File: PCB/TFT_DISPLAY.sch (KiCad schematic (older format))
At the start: 7 parts, among them Q5 MMBT4401-7-F, U17 DT024CTFT(-TS), U18 74HC245, U19 74HC245

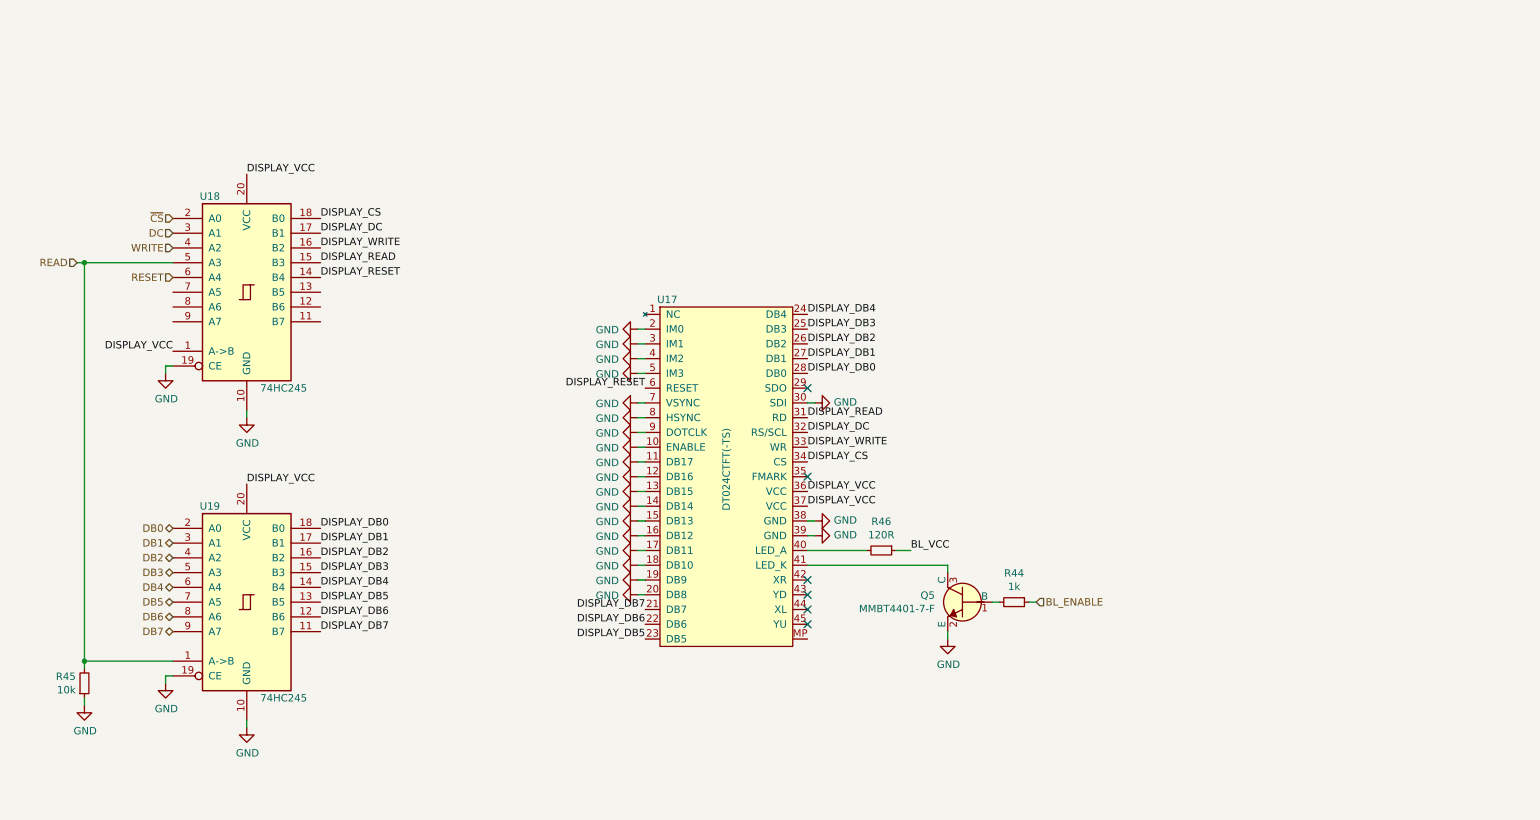
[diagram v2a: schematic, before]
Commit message: Added decoupling and voltage regulation
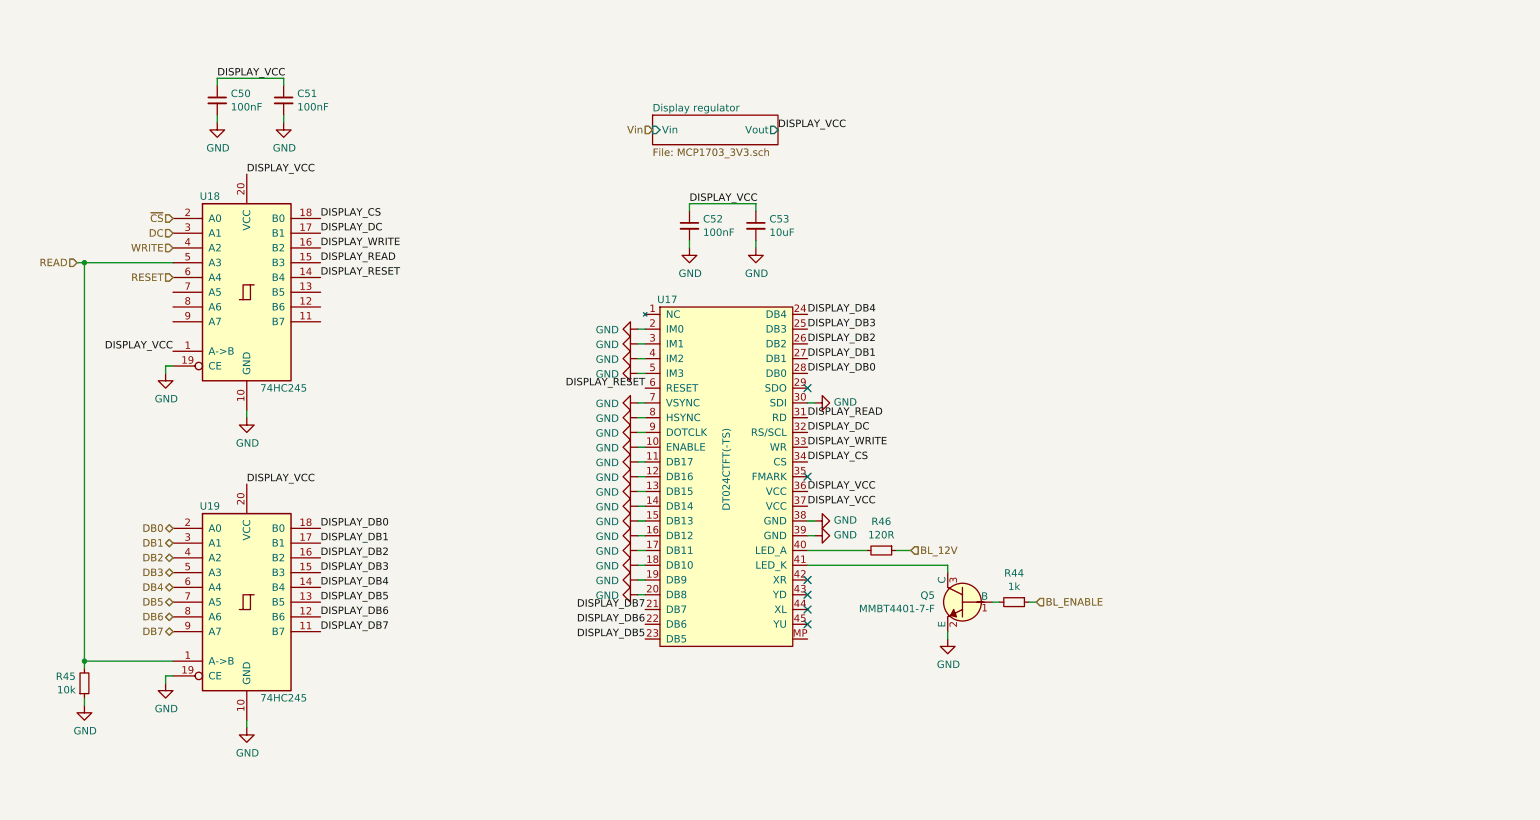
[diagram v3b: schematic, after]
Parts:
- added C50, C51, C52: 100nF, symbol Device:C_Small
- added C53: 10uF, symbol Device:C_Small
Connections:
- net DISPLAY_VCC: now also C50.1, C51.1, C52.1, C53.1
- net GND: now also C50.2, C51.2, C52.2, C53.2
- net BL_VCC renamed BL_12V
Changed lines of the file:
@@
 $Descr A4 11693 8268
 encoding utf-8
-Sheet 27 27
+Sheet 27 28
 Title ""
 Date ""
@@
 NoConn ~ 6850 4750
 NoConn ~ 6850 4850
-Text Label 7550 4350 0    50   ~ 0
-BL_VCC
 $Comp
 L power:GND #PWR0165
@@
 Wire Wire Line
 	6850 4350 7250 4350
+Text Label 6650 1500 0    50   ~ 0
+DISPLAY_VCC
+$Sheet
+S 5800 1400 850  200
+U 5EA9342A
+F0 "Display regulator" 50
+F1 "MCP1703_3V3.sch" 50
+F2 "Vin" I L 5800 1500 50
+F3 "Vout" O R 6650 1500 50
+$EndSheet
+Text HLabel 7550 4350 2    50   Input ~ 0
+BL_12V
+Wire Wire Line
+	2850 1150 3300 1150
+Wire Wire Line
+	2850 1400 2850 1450
+$Comp
+L power:GND #PWR0183
+U 1 1 5EAA8FA4
+P 2850 1450
+F 0 "#PWR0183" H 2850 1200 50  0001 C CNN
+F 1 "GND" H 2855 1277 50  0000 C CNN
+F 2 "" H 2850 1450 50  0001 C CNN
+F 3 "" H 2850 1450 50  0001 C CNN
+	1    2850 1450
+	1    0    0    -1
+$EndComp
+Wire Wire Line
+	2850 1150 2850 1200
+$Comp
+L Device:C_Small C50
+U 1 1 5EAA8F9C
+P 2850 1300
+F 0 "C50" H 2942 1346 50  0000 L CNN
+F 1 "100nF" H 2942 1255 50  0000 L CNN
+F 2 "" H 2850 1300 50  0001 C CNN
+F 3 "~" H 2850 1300 50  0001 C CNN
+	1    2850 1300
+	1    0    0    -1
+$EndComp
+Wire Wire Line
+	3300 1400 3300 1450
+$Comp
+L power:GND #PWR0184
+U 1 1 5EAA64C6
+P 3300 1450
+F 0 "#PWR0184" H 3300 1200 50  0001 C CNN
+F 1 "GND" H 3305 1277 50  0000 C CNN
+F 2 "" H 3300 1450 50  0001 C CNN
+F 3 "" H 3300 1450 50  0001 C CNN
+	1    3300 1450
+	1    0    0    -1
+$EndComp
+Wire Wire Line
+	3300 1150 3300 1200
+Text Label 2850 1150 0    50   ~ 0
+DISPLAY_VCC
+$Comp
+L Device:C_Small C51
+U 1 1 5EAA43F9
+P 3300 1300
+F 0 "C51" H 3392 1346 50  0000 L CNN
+F 1 "100nF" H 3392 1255 50  0000 L CNN
+F 2 "" H 3300 1300 50  0001 C CNN
+F 3 "~" H 3300 1300 50  0001 C CNN
+	1    3300 1300
+	1    0    0    -1
+$EndComp
+Wire Wire Line
+	6050 2000 6500 2000
+Wire Wire Line
+	6050 2250 6050 2300
+$Comp
+L power:GND #PWR0185
+U 1 1 5EAB867A
+P 6050 2300
+F 0 "#PWR0185" H 6050 2050 50  0001 C CNN
+F 1 "GND" H 6055 2127 50  0000 C CNN
+F 2 "" H 6050 2300 50  0001 C CNN
+F 3 "" H 6050 2300 50  0001 C CNN
+	1    6050 2300
+	1    0    0    -1
+$EndComp
+Wire Wire Line
+	6050 2000 6050 2050
+$Comp
+L Device:C_Small C52
+U 1 1 5EAB8681
+P 6050 2150
+F 0 "C52" H 6142 2196 50  0000 L CNN
+F 1 "100nF" H 6142 2105 50  0000 L CNN
+F 2 "" H 6050 2150 50  0001 C CNN
+F 3 "~" H 6050 2150 50  0001 C CNN
+	1    6050 2150
+	1    0    0    -1
+$EndComp
+Wire Wire Line
+	6500 2250 6500 2300
+$Comp
+L power:GND #PWR0186
+U 1 1 5EAB8688
+P 6500 2300
+F 0 "#PWR0186" H 6500 2050 50  0001 C CNN
+F 1 "GND" H 6505 2127 50  0000 C CNN
+F 2 "" H 6500 2300 50  0001 C CNN
+F 3 "" H 6500 2300 50  0001 C CNN
+	1    6500 2300
+	1    0    0    -1
+$EndComp
+Wire Wire Line
+	6500 2000 6500 2050
+Text Label 6050 2000 0    50   ~ 0
+DISPLAY_VCC
+$Comp
+L Device:C_Small C53
+U 1 1 5EAB8690
+P 6500 2150
+F 0 "C53" H 6592 2196 50  0000 L CNN
+F 1 "10uF" H 6592 2105 50  0000 L CNN
+F 2 "" H 6500 2150 50  0001 C CNN
+F 3 "~" H 6500 2150 50  0001 C CNN
+	1    6500 2150
+	1    0    0    -1
+$EndComp
+Text HLabel 5800 1500 0    50   Input ~ 0
+Vin
 $EndSCHEMATC

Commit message: Corrected bus driver MPNs
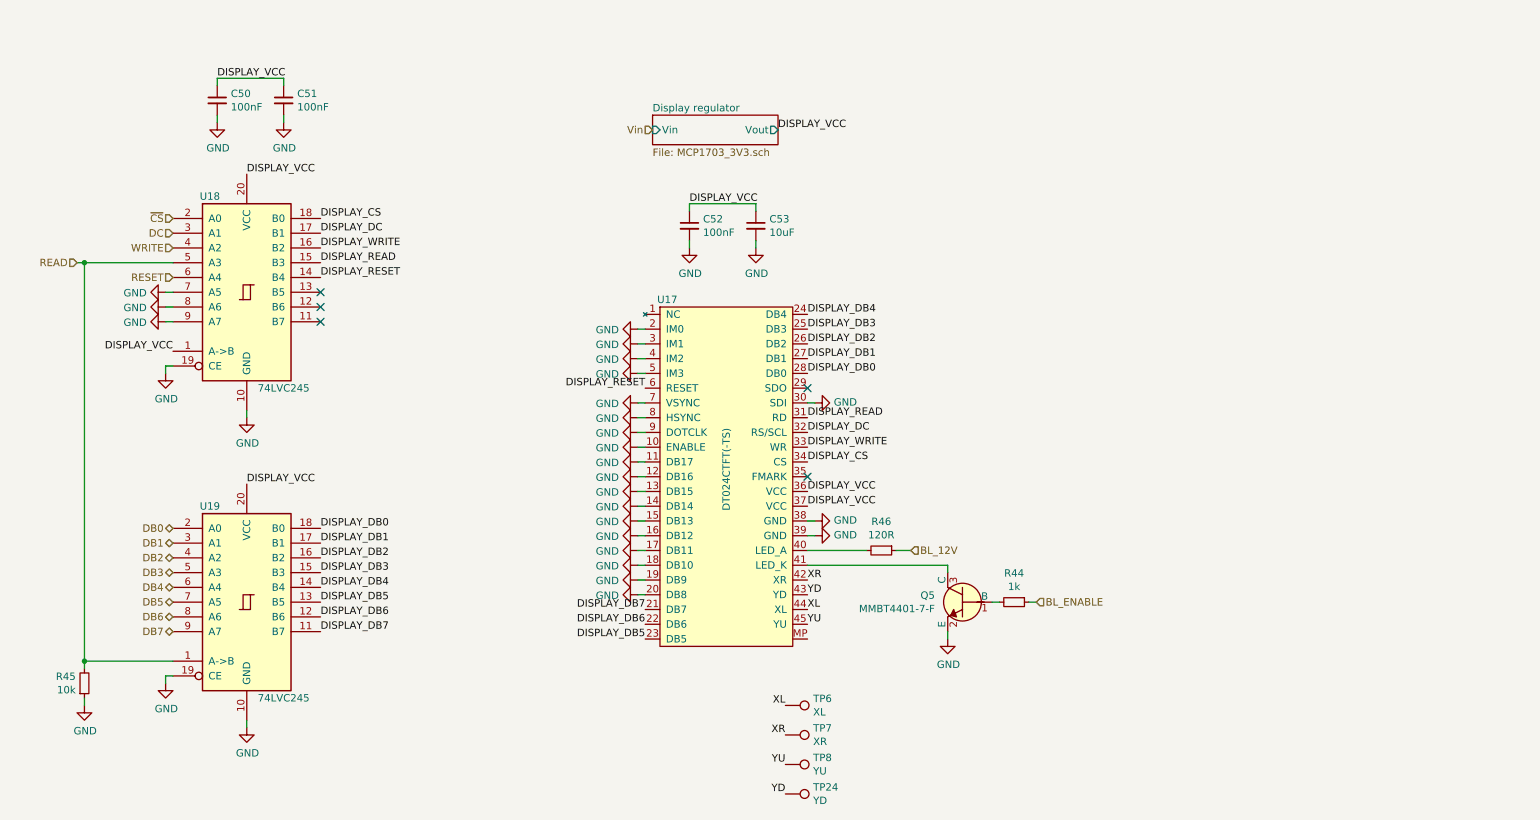
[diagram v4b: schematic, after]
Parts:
- added TP24: YD, symbol Connector:TestPoint
- added TP6: XL, symbol Connector:TestPoint
- added TP7: XR, symbol Connector:TestPoint
- added TP8: YU, symbol Connector:TestPoint
- U18, U19: value 74HC245 -> 74LVC245
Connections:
- net GND: now also U18.7 (A5), U18.8 (A6), U18.9 (A7)
- net XR: now reaches U17.42 (XR)
- net XR: now also TP7.1
- net YD: now reaches U17.43 (YD)
- net YD: now also TP24.1
- net XL: now reaches U17.44 (XL)
- net XL: now also TP6.1
- net YU: now reaches U17.45 (YU)
- net YU: now also TP8.1
- no-connect marks 6 -> 5
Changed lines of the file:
@@
 DISPLAY_VCC
-$Comp
-L 74xx:74HC245 U19
-U 1 1 5E9F8F76
-P 3050 4700
-F 0 "U19" H 2800 5350 50  0000 C CNN
-F 1 "74HC245" H 3300 4050 50  0000 C CNN
-F 2 "" H 3050 4700 50  0001 C CNN
-F 3 "http://www.ti.com/lit/gpn/sn74HC245" H 3050 4700 50  0001 C CNN
-	1    3050 4700
-	1    0    0    -1
-$EndComp
 $Comp
 L power:GND #PWR0158
@@
 P 3050 2600
 F 0 "U18" H 2800 3250 50  0000 C CNN
-F 1 "74HC245" H 3300 1950 50  0000 C CNN
+F 1 "74LVC245" H 3300 1950 50  0000 C CNN
 F 2 "" H 3050 2600 50  0001 C CNN
-F 3 "http://www.ti.com/lit/gpn/sn74HC245" H 3050 2600 50  0001 C CNN
+F 3 "http://www.ti.com/lit/ds/symlink/sn74lvc245a.pdf" H 3050 2600 50  0001 C CNN
 	1    3050 2600
 	1    0    0    -1
@@
 Text Label 2550 3000 2    50   ~ 0
 DISPLAY_VCC
-NoConn ~ 6850 4550
-NoConn ~ 6850 4650
-NoConn ~ 6850 4750
-NoConn ~ 6850 4850
 $Comp
 L power:GND #PWR0165
@@
 Text HLabel 5800 1500 0    50   Input ~ 0
 Vin
+$Comp
+L 74xx:74HC245 U19
+U 1 1 5E9F8F76
+P 3050 4700
+F 0 "U19" H 2800 5350 50  0000 C CNN
+F 1 "74LVC245" H 3300 4050 50  0000 C CNN
+F 2 "" H 3050 4700 50  0001 C CNN
+F 3 "http://www.ti.com/lit/ds/symlink/sn74lvc245a.pdf" H 3050 4700 50  0001 C CNN
+	1    3050 4700
+	1    0    0    -1
+$EndComp
+$Comp
+L Connector:TestPoint TP7
+U 1 1 5EADCDE5
+P 6700 5600
+F 0 "TP7" V 6654 5788 50  0000 L CNN
+F 1 "XR" V 6745 5788 50  0000 L CNN
+F 2 "" H 6900 5600 50  0001 C CNN
+F 3 "~" H 6900 5600 50  0001 C CNN
+	1    6700 5600
+	0    1    1    0
+$EndComp
+$Comp
+L Connector:TestPoint TP6
+U 1 1 5EADD33B
+P 6700 5400
+F 0 "TP6" V 6654 5588 50  0000 L CNN
+F 1 "XL" V 6745 5588 50  0000 L CNN
+F 2 "" H 6900 5400 50  0001 C CNN
+F 3 "~" H 6900 5400 50  0001 C CNN
+	1    6700 5400
+	0    1    1    0
+$EndComp
+$Comp
+L Connector:TestPoint TP8
+U 1 1 5EADD59A
+P 6700 5800
+F 0 "TP8" V 6654 5988 50  0000 L CNN
+F 1 "YU" V 6745 5988 50  0000 L CNN
+F 2 "" H 6900 5800 50  0001 C CNN
+F 3 "~" H 6900 5800 50  0001 C CNN
+	1    6700 5800
+	0    1    1    0
+$EndComp
+$Comp
+L Connector:TestPoint TP24
+U 1 1 5EADD7EA
+P 6700 6000
+F 0 "TP24" V 6654 6188 50  0000 L CNN
+F 1 "YD" V 6745 6188 50  0000 L CNN
+F 2 "" H 6900 6000 50  0001 C CNN
+F 3 "~" H 6900 6000 50  0001 C CNN
+	1    6700 6000
+	0    1    1    0
+$EndComp
+Text Label 6850 4550 0    50   ~ 0
+XR
+Text Label 6850 4650 0    50   ~ 0
+YD
+Text Label 6850 4750 0    50   ~ 0
+XL
+Text Label 6850 4850 0    50   ~ 0
+YU
+Text Label 6700 5600 2    50   ~ 0
+XR
+Text Label 6700 6000 2    50   ~ 0
+YD
+Text Label 6700 5400 2    50   ~ 0
+XL
+Text Label 6700 5800 2    50   ~ 0
+YU
+NoConn ~ 3550 2600
+NoConn ~ 3550 2700
+NoConn ~ 3550 2800
+$Comp
+L power:GND #PWR?
+U 1 1 5EAFC8BD
+P 2500 2600
+F 0 "#PWR?" H 2500 2350 50  0001 C CNN
+F 1 "GND" V 2505 2472 50  0000 R CNN
+F 2 "" H 2500 2600 50  0001 C CNN
+F 3 "" H 2500 2600 50  0001 C CNN
+	1    2500 2600
+	0    1    1    0
+$EndComp
+$Comp
+L power:GND #PWR?
+U 1 1 5EAFCB8D
+P 2500 2700
+F 0 "#PWR?" H 2500 2450 50  0001 C CNN
+F 1 "GND" V 2505 2572 50  0000 R CNN
+F 2 "" H 2500 2700 50  0001 C CNN
+F 3 "" H 2500 2700 50  0001 C CNN
+	1    2500 2700
+	0    1    1    0
+$EndComp
+$Comp
+L power:GND #PWR?
+U 1 1 5EAFCCE4
+P 2500 2800
+F 0 "#PWR?" H 2500 2550 50  0001 C CNN
+F 1 "GND" V 2505 2672 50  0000 R CNN
+F 2 "" H 2500 2800 50  0001 C CNN
+F 3 "" H 2500 2800 50  0001 C CNN
+	1    2500 2800
+	0    1    1    0
+$EndComp
+Wire Wire Line
+	2500 2800 2550 2800
+Wire Wire Line
+	2500 2700 2550 2700
+Wire Wire Line
+	2500 2600 2550 2600
 $EndSCHEMATC

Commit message: Added virtual display module and assigned FPC connector footprint
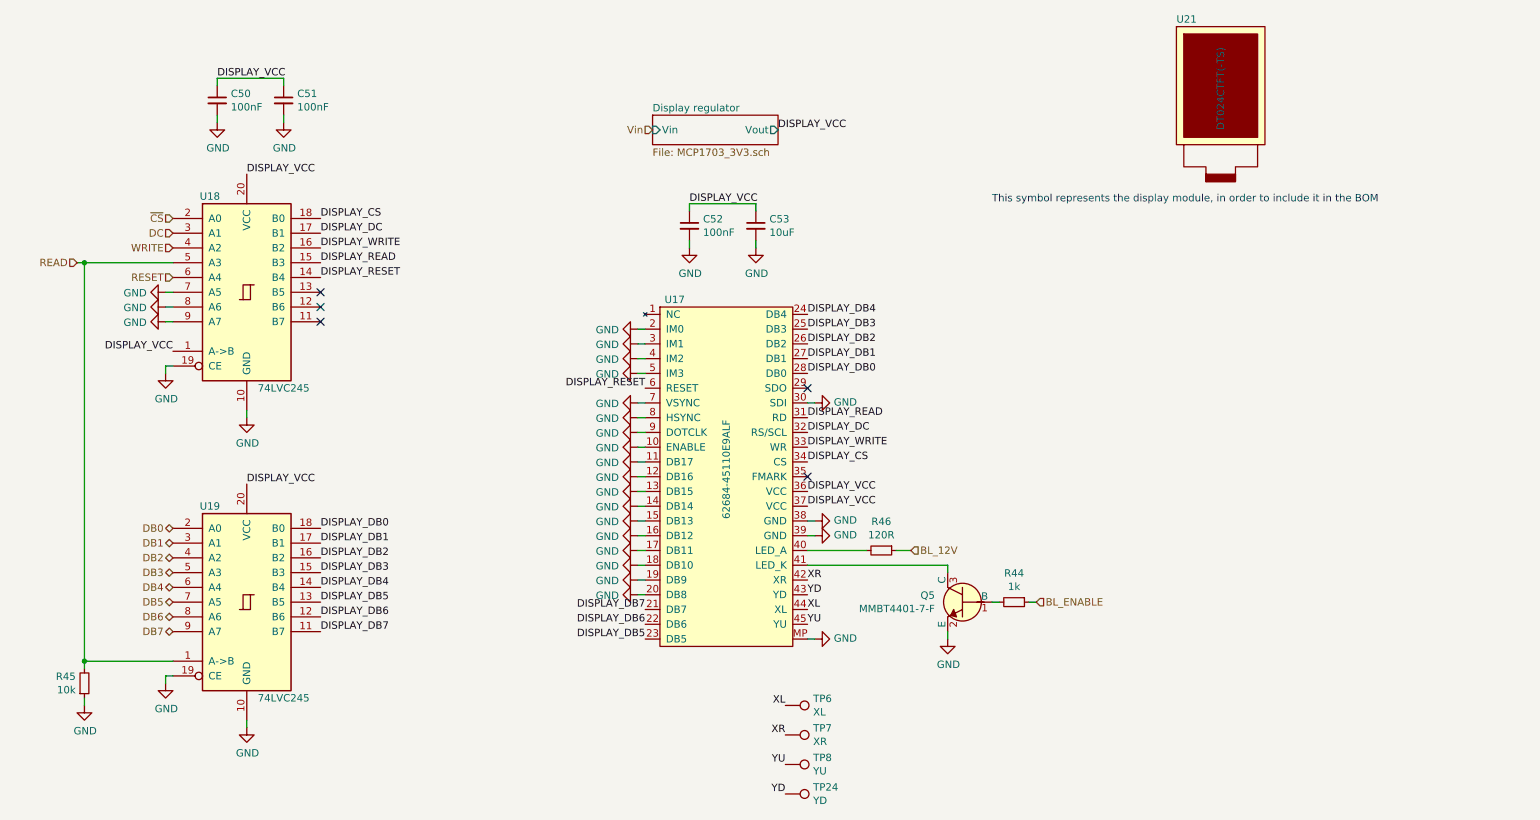
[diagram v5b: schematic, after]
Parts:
- added U21: DT024CTFT(-TS), symbol custom:VIRTUAL_DISPLAY
- U17: value DT024CTFT(-TS) -> 62684-45110E9ALF; footprint (none) -> custom:62684-45110E9ALF
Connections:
- net GND: now also U17.MP
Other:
- note added: "This symbol represents the display module, in order to include it in the BOM"
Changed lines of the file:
@@
 DB0
-$Comp
-L custom:DT024CTFT(-TS) U17
-U 1 1 5E9C83A4
-P 6300 3800
-F 0 "U17" H 5900 4950 50  0000 C CNN
-F 1 "DT024CTFT(-TS)" V 6300 3800 50  0000 C CNN
-F 2 "" H 6200 3950 50  0001 C CNN
-F 3 "https://cdn.displaytech-us.com/sites/default/files/display-data-sheet/DT024CTFT-v10_0.pdf" H 6200 3950 50  0001 C CNN
-	1    6300 3800
-	1    0    0    -1
-$EndComp
 $Comp
 L dk_Transistors-Bipolar-BJT-Single:MMBT4401-7-F Q5
@@
 NoConn ~ 3550 2800
 $Comp
-L power:GND #PWR?
+L power:GND #PWR0191
 U 1 1 5EAFC8BD
 P 2500 2600
-F 0 "#PWR?" H 2500 2350 50  0001 C CNN
+F 0 "#PWR0191" H 2500 2350 50  0001 C CNN
 F 1 "GND" V 2505 2472 50  0000 R CNN
 F 2 "" H 2500 2600 50  0001 C CNN
@@
 $EndComp
 $Comp
-L power:GND #PWR?
+L power:GND #PWR0192
 U 1 1 5EAFCB8D
 P 2500 2700
-F 0 "#PWR?" H 2500 2450 50  0001 C CNN
+F 0 "#PWR0192" H 2500 2450 50  0001 C CNN
 F 1 "GND" V 2505 2572 50  0000 R CNN
 F 2 "" H 2500 2700 50  0001 C CNN
@@
 $EndComp
 $Comp
-L power:GND #PWR?
+L power:GND #PWR0193
 U 1 1 5EAFCCE4
 P 2500 2800
-F 0 "#PWR?" H 2500 2550 50  0001 C CNN
+F 0 "#PWR0193" H 2500 2550 50  0001 C CNN
 F 1 "GND" V 2505 2672 50  0000 R CNN
 F 2 "" H 2500 2800 50  0001 C CNN
@@
 Wire Wire Line
 	2500 2600 2550 2600
+$Comp
+L custom:DT024CTFT(-TS) U17
+U 1 1 5E95B360
+P 6300 3800
+F 0 "U17" H 5950 4950 50  0000 C CNN
+F 1 "62684-45110E9ALF" V 6300 3800 50  0000 C CNN
+F 2 "custom:62684-45110E9ALF" H 6200 3950 50  0001 C CNN
+F 3 "https://cdn.amphenol-icc.com/media/wysiwyg/files/drawing/62684.pdf?__cf_chl_jschl_tk__=803acbf1fe55cff0ce3c0997063ab13baf380f8e-1586799606-0-AWj8eUdRD6VeqKIGOzk8_7ESWh-l-Nfv72sYbynJqjU-dUbsmngP34dquq2aBN_2_g14FJmOfnMJLLjyATnc-xvODXDum6C81rxij_OuVs93oeXHSY4u152qJd17kfaml1TAd7PfKT-9VsSBUM6y7EgcLufJOL2ihQ5GNpEeVhldnUN6WOCwqJv1c8deuqFqfu2dVhn1Q6fQGgyqCqlHsQH_xsQDoHi2sZFqqZBKQiceqeLE0FPl0fWnJVsE9ZYdTpUyth72B1TCrFFS1O4VaX2xwd-gpPLy0qbyRll2OjvcdP_02UcTTu_coU3l3kzPoDAVWb_BdgZp6LcaPbu9BGJHEVVpIKZrvc8vczxr6TAHuj3eoSFi5lPhJ2GDnriFIg" H 6200 3950 50  0001 C CNN
+	1    6300 3800
+	1    0    0    -1
+$EndComp
+$Comp
+L power:GND #PWR0194
+U 1 1 5E95DA17
+P 6900 4950
+F 0 "#PWR0194" H 6900 4700 50  0001 C CNN
+F 1 "GND" V 6905 4822 50  0000 R CNN
+F 2 "" H 6900 4950 50  0001 C CNN
+F 3 "" H 6900 4950 50  0001 C CNN
+	1    6900 4950
+	0    -1   -1   0
+$EndComp
+Wire Wire Line
+	6900 4950 6850 4950
+$Comp
+L custom:VIRTUAL_DISPLAY U21
+U 1 1 5E968691
+P 9650 1200
+F 0 "U21" H 9350 1650 50  0000 L CNN
+F 1 "DT024CTFT(-TS)" V 9650 900 50  0000 L CNN
+F 2 "" H 9650 1200 50  0001 C CNN
+F 3 "https://cdn.displaytech-us.com/sites/default/files/display-data-sheet/DT024CTFT-v10_0.pdf" H 9650 1200 50  0001 C CNN
+	1    9650 1200
+	1    0    0    -1
+$EndComp
+Text Notes 8100 2000 0    50   ~ 0
+This symbol represents the display module, in order to include it in the BOM
 $EndSCHEMATC

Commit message: Added display footprint
This includes the area for placing the display, ribbon slot and guide for placing the FPC
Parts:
- U21: footprint (none) -> custom:DT024CTFT-(TS)
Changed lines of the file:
@@
 F 0 "U21" H 9350 1650 50  0000 L CNN
 F 1 "DT024CTFT(-TS)" V 9650 900 50  0000 L CNN
-F 2 "" H 9650 1200 50  0001 C CNN
+F 2 "custom:DT024CTFT-(TS)" H 9650 1200 50  0001 C CNN
 F 3 "https://cdn.displaytech-us.com/sites/default/files/display-data-sheet/DT024CTFT-v10_0.pdf" H 9650 1200 50  0001 C CNN
 	1    9650 1200
